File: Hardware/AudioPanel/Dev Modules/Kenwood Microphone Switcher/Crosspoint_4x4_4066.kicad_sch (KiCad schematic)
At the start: 53 parts, among them U201 4066, U202 4066, U203 4066, U204 4066, U205 74HC14, U206 74HC14, U207 74HC14

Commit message: Changed LEDs to 0603 SMDs
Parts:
- D201, D202, D203, D204, D205, D206, D207, D208, D209, D210, D211, D212, D213, D214, D215, D216: footprint LED_THT:LED_D5.0mm -> LED_SMD:LED_0603_1608Metric
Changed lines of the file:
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@@
 			)
 		)
-		(property "Footprint" "LED_THT:LED_D5.0mm"
+		(property "Footprint" "LED_SMD:LED_0603_1608Metric"
 			(at 295.91 105.41 0)
 			(effects
@@
 			)
 		)
-		(property "Footprint" "LED_THT:LED_D5.0mm"
+		(property "Footprint" "LED_SMD:LED_0603_1608Metric"
 			(at 295.91 149.86 0)
 			(effects
@@
 			)
 		)
-		(property "Footprint" "LED_THT:LED_D5.0mm"
+		(property "Footprint" "LED_SMD:LED_0603_1608Metric"
 			(at 295.91 142.24 0)
 			(effects
@@
 			)
 		)
-		(property "Footprint" "LED_THT:LED_D5.0mm"
+		(property "Footprint" "LED_SMD:LED_0603_1608Metric"
 			(at 295.91 69.85 0)
 			(effects
@@
 			)
 		)
-		(property "Footprint" "LED_THT:LED_D5.0mm"
+		(property "Footprint" "LED_SMD:LED_0603_1608Metric"
 			(at 295.91 90.17 0)
 			(effects
@@
 			)
 		)
-		(property "Footprint" "LED_THT:LED_D5.0mm"
+		(property "Footprint" "LED_SMD:LED_0603_1608Metric"
 			(at 295.91 120.65 0)
 			(effects
@@
 			)
 		)
-		(property "Footprint" "LED_THT:LED_D5.0mm"
+		(property "Footprint" "LED_SMD:LED_0603_1608Metric"
 			(at 295.91 97.79 0)
 			(effects
@@
 			)
 		)
-		(property "Footprint" "LED_THT:LED_D5.0mm"
+		(property "Footprint" "LED_SMD:LED_0603_1608Metric"
 			(at 295.91 62.23 0)
 			(effects
@@
 			)
 		)
-		(property "Footprint" "LED_THT:LED_D5.0mm"
+		(property "Footprint" "LED_SMD:LED_0603_1608Metric"
 			(at 295.91 157.48 0)
 			(effects
@@
 			)
 		)
-		(property "Footprint" "LED_THT:LED_D5.0mm"
+		(property "Footprint" "LED_SMD:LED_0603_1608Metric"
 			(at 295.91 113.03 0)
 			(effects
@@
 			)
 		)
-		(property "Footprint" "LED_THT:LED_D5.0mm"
+		(property "Footprint" "LED_SMD:LED_0603_1608Metric"
 			(at 295.91 31.75 0)
 			(effects
@@
 			)
 		)
-		(property "Footprint" "LED_THT:LED_D5.0mm"
+		(property "Footprint" "LED_SMD:LED_0603_1608Metric"
 			(at 295.91 54.61 0)
 			(effects
@@
 			)
 		)
-		(property "Footprint" "LED_THT:LED_D5.0mm"
+		(property "Footprint" "LED_SMD:LED_0603_1608Metric"
 			(at 295.91 46.99 0)
 			(effects
@@
 			)
 		)
-		(property "Footprint" "LED_THT:LED_D5.0mm"
+		(property "Footprint" "LED_SMD:LED_0603_1608Metric"
 			(at 295.91 82.55 0)
 			(effects
@@
 			)
 		)
-		(property "Footprint" "LED_THT:LED_D5.0mm"
+		(property "Footprint" "LED_SMD:LED_0603_1608Metric"
 			(at 295.91 39.37 0)
 			(effects
@@
 			)
 		)
-		(property "Footprint" "LED_THT:LED_D5.0mm"
+		(property "Footprint" "LED_SMD:LED_0603_1608Metric"
 			(at 295.91 134.62 0)
 			(effects

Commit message: Changed resistor arrays to SMD
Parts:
- RN201, RN202, RN203, RN204: footprint Resistor_THT:R_Array_SIP5 -> Resistor_SMD:R_Array_Concave_4x0402
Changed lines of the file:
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@@
 			)
 		)
-		(property "Footprint" "Resistor_THT:R_Array_SIP5"
+		(property "Footprint" "Resistor_SMD:R_Array_Concave_4x0402"
 			(at 167.64 52.832 90)
 			(effects
@@
 			)
 		)
-		(property "Footprint" "Resistor_THT:R_Array_SIP5"
+		(property "Footprint" "Resistor_SMD:R_Array_Concave_4x0402"
 			(at 167.64 47.752 90)
 			(effects
@@
 			)
 		)
-		(property "Footprint" "Resistor_THT:R_Array_SIP5"
+		(property "Footprint" "Resistor_SMD:R_Array_Concave_4x0402"
 			(at 167.64 27.432 90)
 			(effects
@@
 			)
 		)
-		(property "Footprint" "Resistor_THT:R_Array_SIP5"
+		(property "Footprint" "Resistor_SMD:R_Array_Concave_4x0402"
 			(at 167.64 32.512 90)
 			(effects
@@
 			)
 		)
-		(property "Footprint" "Resistor_THT:R_Array_SIP5"
+		(property "Footprint" "Resistor_SMD:R_Array_Concave_4x0402"
 			(at 167.64 40.132 90)
 			(effects
@@
 			)
 		)
-		(property "Footprint" "Resistor_THT:R_Array_SIP5"
+		(property "Footprint" "Resistor_SMD:R_Array_Concave_4x0402"
 			(at 167.64 65.532 90)
 			(effects
@@
 			)
 		)
-		(property "Footprint" "Resistor_THT:R_Array_SIP5"
+		(property "Footprint" "Resistor_SMD:R_Array_Concave_4x0402"
 			(at 167.64 37.592 90)
 			(effects
@@
 			)
 		)
-		(property "Footprint" "Resistor_THT:R_Array_SIP5"
+		(property "Footprint" "Resistor_SMD:R_Array_Concave_4x0402"
 			(at 167.64 62.992 90)
 			(effects
@@
 			)
 		)
-		(property "Footprint" "Resistor_THT:R_Array_SIP5"
+		(property "Footprint" "Resistor_SMD:R_Array_Concave_4x0402"
 			(at 167.64 45.212 90)
 			(effects
@@
 			)
 		)
-		(property "Footprint" "Resistor_THT:R_Array_SIP5"
+		(property "Footprint" "Resistor_SMD:R_Array_Concave_4x0402"
 			(at 167.64 29.972 90)
 			(effects
@@
 			)
 		)
-		(property "Footprint" "Resistor_THT:R_Array_SIP5"
+		(property "Footprint" "Resistor_SMD:R_Array_Concave_4x0402"
 			(at 167.64 57.912 90)
 			(effects
@@
 			)
 		)
-		(property "Footprint" "Resistor_THT:R_Array_SIP5"
+		(property "Footprint" "Resistor_SMD:R_Array_Concave_4x0402"
 			(at 167.64 35.052 90)
 			(effects
@@
 			)
 		)
-		(property "Footprint" "Resistor_THT:R_Array_SIP5"
+		(property "Footprint" "Resistor_SMD:R_Array_Concave_4x0402"
 			(at 167.64 50.292 90)
 			(effects
@@
 			)
 		)
-		(property "Footprint" "Resistor_THT:R_Array_SIP5"
+		(property "Footprint" "Resistor_SMD:R_Array_Concave_4x0402"
 			(at 167.64 42.672 90)
 			(effects
@@
 			)
 		)
-		(property "Footprint" "Resistor_THT:R_Array_SIP5"
+		(property "Footprint" "Resistor_SMD:R_Array_Concave_4x0402"
 			(at 167.64 60.452 90)
 			(effects
@@
 			)
 		)
-		(property "Footprint" "Resistor_THT:R_Array_SIP5"
+		(property "Footprint" "Resistor_SMD:R_Array_Concave_4x0402"
 			(at 167.64 55.372 90)
 			(effects

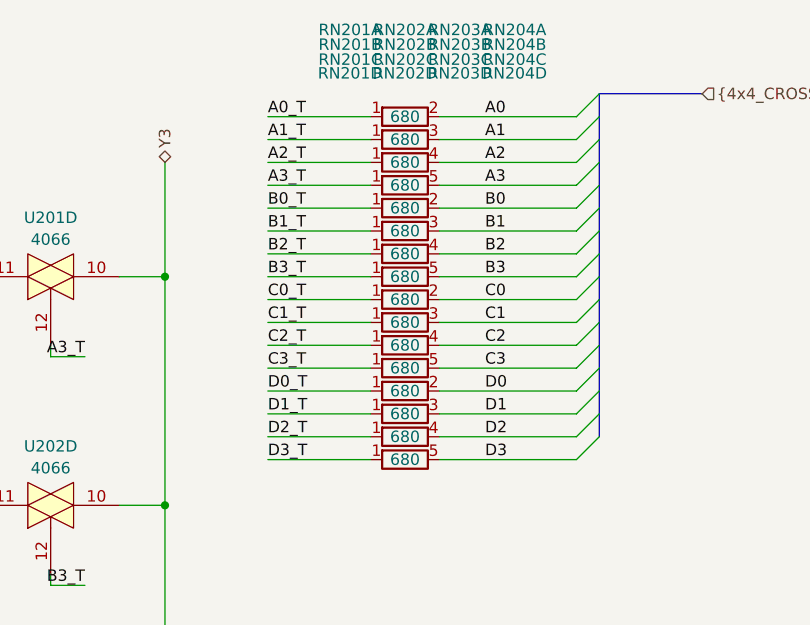
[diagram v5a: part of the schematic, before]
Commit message: Finished assigning footprints
No errors in PCB import, woo!
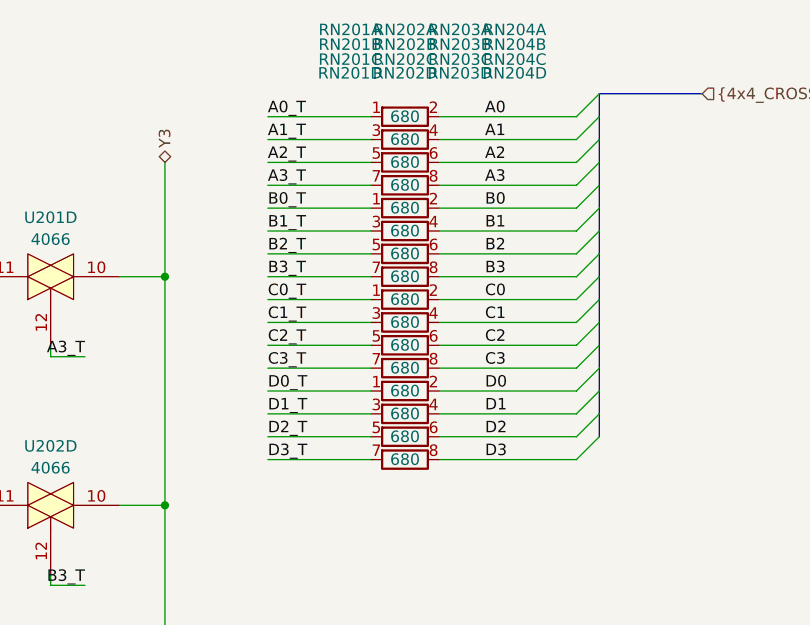
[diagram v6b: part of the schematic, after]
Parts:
- RN201, RN202, RN203, RN204: footprint Resistor_SMD:R_Array_Concave_4x0402 -> Resistor_SMD:R_Array_Convex_4x1206; symbol Device:R_Network04_Split -> Library_MicSwitcher:R_Network04_Split
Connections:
- net A1: now also RN201.4; no longer RN201.3 (R2.2)
- net A1_T: now also RN201.3; no longer RN201.1 (R1)
- net A2: now also RN201.6; no longer RN201.4 (R3.2)
- net A2_T: now also RN201.5; no longer RN201.1 (R1)
- net A3: now also RN201.8; no longer RN201.5 (R4.2)
- net A3_T: now also RN201.7; no longer RN201.1 (R1)
- net B1: now also RN202.4; no longer RN202.3 (R2.2)
- net B1_T: now also RN202.3; no longer RN202.1 (R1)
- net B2: now also RN202.6; no longer RN202.4 (R3.2)
- net B2_T: now also RN202.5; no longer RN202.1 (R1)
- net B3: now also RN202.8; no longer RN202.5 (R4.2)
- net B3_T: now also RN202.7; no longer RN202.1 (R1)
- net C1: now also RN203.4; no longer RN203.3 (R2.2)
- net C1_T: now also RN203.3; no longer RN203.1 (R1)
- net C2: now also RN203.6; no longer RN203.4 (R3.2)
- net C2_T: now also RN203.5; no longer RN203.1 (R1)
- net C3: now also RN203.8; no longer RN203.5 (R4.2)
- net C3_T: now also RN203.7; no longer RN203.1 (R1)
- net D1: now also RN204.4; no longer RN204.3 (R2.2)
- net D1_T: now also RN204.3; no longer RN204.1 (R1)
- net D2: now also RN204.6; no longer RN204.4 (R3.2)
- net D2_T: now also RN204.5; no longer RN204.1 (R1)
- net D3: now also RN204.8; no longer RN204.5 (R4.2)
- net D3_T: now also RN204.7; no longer RN204.1 (R1)
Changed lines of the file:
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@@
 	)
 	(symbol
-		(lib_id "Device:R_Network04_Split")
+		(lib_id "Library_MicSwitcher:R_Network04_Split")
 		(at 167.64 50.8 90)
 		(unit 3)
@@
 			)
 		)
-		(property "Footprint" "Resistor_SMD:R_Array_Concave_4x0402"
+		(property "Footprint" "Resistor_SMD:R_Array_Convex_4x1206"
 			(at 167.64 52.832 90)
 			(effects
@@
 		(pin "2"
 		)
+		(pin "7"
+		)
+		(pin "6"
+		)
+		(pin "8"
+		)
 		(instances
 			(project "Kenwood Microphone Switcher"
@@
 	)
 	(symbol
-		(lib_id "Device:R_Network04_Split")
+		(lib_id "Library_MicSwitcher:R_Network04_Split")
 		(at 167.64 45.72 90)
 		(unit 1)
@@
 			)
 		)
-		(property "Footprint" "Resistor_SMD:R_Array_Concave_4x0402"
+		(property "Footprint" "Resistor_SMD:R_Array_Convex_4x1206"
 			(at 167.64 47.752 90)
 			(effects
@@
 		(pin "2"
 		)
+		(pin "8"
+		)
+		(pin "6"
+		)
+		(pin "7"
+		)
 		(instances
 			(project "Kenwood Microphone Switcher"
@@
 	)
 	(symbol
-		(lib_id "Device:R_Network04_Split")
+		(lib_id "Library_MicSwitcher:R_Network04_Split")
 		(at 167.64 25.4 90)
 		(unit 1)
@@
 			)
 		)
-		(property "Footprint" "Resistor_SMD:R_Array_Concave_4x0402"
+		(property "Footprint" "Resistor_SMD:R_Array_Convex_4x1206"
 			(at 167.64 27.432 90)
 			(effects
@@
 		(pin "2"
 		)
+		(pin "6"
+		)
+		(pin "8"
+		)
+		(pin "7"
+		)
 		(instances
 			(project ""
@@
 	)
 	(symbol
-		(lib_id "Device:R_Network04_Split")
+		(lib_id "Library_MicSwitcher:R_Network04_Split")
 		(at 167.64 30.48 90)
 		(unit 3)
@@
 			)
 		)
-		(property "Footprint" "Resistor_SMD:R_Array_Concave_4x0402"
+		(property "Footprint" "Resistor_SMD:R_Array_Convex_4x1206"
 			(at 167.64 32.512 90)
 			(effects
@@
 		(pin "2"
 		)
+		(pin "8"
+		)
+		(pin "7"
+		)
+		(pin "6"
+		)
 		(instances
 			(project ""
@@
 	)
 	(symbol
-		(lib_id "Device:R_Network04_Split")
+		(lib_id "Library_MicSwitcher:R_Network04_Split")
 		(at 167.64 38.1 90)
 		(unit 2)
@@
 			)
 		)
-		(property "Footprint" "Resistor_SMD:R_Array_Concave_4x0402"
+		(property "Footprint" "Resistor_SMD:R_Array_Convex_4x1206"
 			(at 167.64 40.132 90)
 			(effects
@@
 		(pin "2"
 		)
+		(pin "7"
+		)
+		(pin "6"
+		)
+		(pin "8"
+		)
 		(instances
 			(project "Kenwood Microphone Switcher"
@@
 	)
 	(symbol
-		(lib_id "Device:R_Network04_Split")
+		(lib_id "Library_MicSwitcher:R_Network04_Split")
 		(at 167.64 63.5 90)
 		(unit 4)
@@
 			)
 		)
-		(property "Footprint" "Resistor_SMD:R_Array_Concave_4x0402"
+		(property "Footprint" "Resistor_SMD:R_Array_Convex_4x1206"
 			(at 167.64 65.532 90)
 			(effects
@@
 		(pin "2"
 		)
+		(pin "8"
+		)
+		(pin "6"
+		)
+		(pin "7"
+		)
 		(instances
 			(project "Kenwood Microphone Switcher"
@@
 	)
 	(symbol
-		(lib_id "Device:R_Network04_Split")
+		(lib_id "Library_MicSwitcher:R_Network04_Split")
 		(at 167.64 35.56 90)
 		(unit 1)
@@
 			)
 		)
-		(property "Footprint" "Resistor_SMD:R_Array_Concave_4x0402"
+		(property "Footprint" "Resistor_SMD:R_Array_Convex_4x1206"
 			(at 167.64 37.592 90)
 			(effects
@@
 		(pin "2"
 		)
+		(pin "6"
+		)
+		(pin "7"
+		)
+		(pin "8"
+		)
 		(instances
 			(project "Kenwood Microphone Switcher"
@@
 		(dnp no)
 		(fields_autoplaced yes)
-		(property "Reference" "#PWR0215"
+		(property "Reference" "#PWR0213"
 			(at 311.15 172.72 0)
 			(effects
@@
 			(project "Kenwood Microphone Switcher"
 				(path "/19b5c763-986e-434c-80ff-b1ac9c189e0e/08a77cad-86d7-4f50-8517-cb6e2e11f987"
-					(reference "#PWR0215")
+					(reference "#PWR0213")
 					(unit 1)
 				)
@@
 	)
 	(symbol
-		(lib_id "Device:R_Network04_Split")
+		(lib_id "Library_MicSwitcher:R_Network04_Split")
 		(at 167.64 60.96 90)
 		(unit 3)
@@
 			)
 		)
-		(property "Footprint" "Resistor_SMD:R_Array_Concave_4x0402"
+		(property "Footprint" "Resistor_SMD:R_Array_Convex_4x1206"
 			(at 167.64 62.992 90)
 			(effects
@@
 		(pin "2"
 		)
+		(pin "6"
+		)
+		(pin "8"
+		)
+		(pin "7"
+		)
 		(instances
 			(project "Kenwood Microphone Switcher"
@@
 	)
 	(symbol
-		(lib_id "Device:R_Network04_Split")
+		(lib_id "Library_MicSwitcher:R_Network04_Split")
 		(at 167.64 43.18 90)
 		(unit 4)
@@
 			)
 		)
-		(property "Footprint" "Resistor_SMD:R_Array_Concave_4x0402"
+		(property "Footprint" "Resistor_SMD:R_Array_Convex_4x1206"
 			(at 167.64 45.212 90)
 			(effects
@@
 		(pin "2"
 		)
+		(pin "7"
+		)
+		(pin "6"
+		)
+		(pin "8"
+		)
 		(instances
 			(project "Kenwood Microphone Switcher"
@@
 	)
 	(symbol
-		(lib_id "Device:R_Network04_Split")
+		(lib_id "Library_MicSwitcher:R_Network04_Split")
 		(at 167.64 27.94 90)
 		(unit 2)
@@
 			)
 		)
-		(property "Footprint" "Resistor_SMD:R_Array_Concave_4x0402"
+		(property "Footprint" "Resistor_SMD:R_Array_Convex_4x1206"
 			(at 167.64 29.972 90)
 			(effects
@@
 		(pin "2"
 		)
+		(pin "6"
+		)
+		(pin "7"
+		)
+		(pin "8"
+		)
 		(instances
 			(project ""
@@
 	)
 	(symbol
-		(lib_id "Device:R_Network04_Split")
+		(lib_id "Library_MicSwitcher:R_Network04_Split")
 		(at 167.64 55.88 90)
 		(unit 1)
@@
 			)
 		)
-		(property "Footprint" "Resistor_SMD:R_Array_Concave_4x0402"
+		(property "Footprint" "Resistor_SMD:R_Array_Convex_4x1206"
 			(at 167.64 57.912 90)
 			(effects
@@
 		(pin "2"
 		)
+		(pin "6"
+		)
+		(pin "8"
+		)
+		(pin "7"
+		)
 		(instances
 			(project "Kenwood Microphone Switcher"
@@
 	)
 	(symbol
-		(lib_id "Device:R_Network04_Split")
+		(lib_id "Library_MicSwitcher:R_Network04_Split")
 		(at 167.64 33.02 90)
 		(unit 4)
@@
 			)
 		)
-		(property "Footprint" "Resistor_SMD:R_Array_Concave_4x0402"
+		(property "Footprint" "Resistor_SMD:R_Array_Convex_4x1206"
 			(at 167.64 35.052 90)
 			(effects
@@
 		(pin "2"
 		)
+		(pin "8"
+		)
+		(pin "6"
+		)
+		(pin "7"
+		)
 		(instances
 			(project ""
@@
 		(dnp no)
 		(fields_autoplaced yes)
-		(property "Reference" "#PWR0213"
+		(property "Reference" "#PWR0211"
 			(at 311.15 69.85 0)
 			(effects
@@
 			(project "Kenwood Microphone Switcher"
 				(path "/19b5c763-986e-434c-80ff-b1ac9c189e0e/08a77cad-86d7-4f50-8517-cb6e2e11f987"
-					(reference "#PWR0213")
+					(reference "#PWR0211")
 					(unit 1)
 				)
@@
 	)
 	(symbol
-		(lib_id "Device:R_Network04_Split")
+		(lib_id "Library_MicSwitcher:R_Network04_Split")
 		(at 167.64 48.26 90)
 		(unit 2)
@@
 			)
 		)
-		(property "Footprint" "Resistor_SMD:R_Array_Concave_4x0402"
+		(property "Footprint" "Resistor_SMD:R_Array_Convex_4x1206"
 			(at 167.64 50.292 90)
 			(effects
@@
 		(pin "2"
 		)
+		(pin "6"
+		)
+		(pin "7"
+		)
+		(pin "8"
+		)
 		(instances
 			(project "Kenwood Microphone Switcher"
@@
 	)
 	(symbol
-		(lib_id "Device:R_Network04_Split")
+		(lib_id "Library_MicSwitcher:R_Network04_Split")
 		(at 167.64 40.64 90)
 		(unit 3)
@@
 			)
 		)
-		(property "Footprint" "Resistor_SMD:R_Array_Concave_4x0402"
+		(property "Footprint" "Resistor_SMD:R_Array_Convex_4x1206"
 			(at 167.64 42.672 90)
 			(effects
@@
 		(pin "2"
 		)
+		(pin "6"
+		)
+		(pin "8"
+		)
+		(pin "7"
+		)
 		(instances
 			(project "Kenwood Microphone Switcher"
@@
 	)
 	(symbol
-		(lib_id "Device:R_Network04_Split")
+		(lib_id "Library_MicSwitcher:R_Network04_Split")
 		(at 167.64 58.42 90)
 		(unit 2)
@@
 			)
 		)
-		(property "Footprint" "Resistor_SMD:R_Array_Concave_4x0402"
+		(property "Footprint" "Resistor_SMD:R_Array_Convex_4x1206"
 			(at 167.64 60.452 90)
 			(effects
@@
 		(pin "2"
 		)
+		(pin "7"
+		)
+		(pin "6"
+		)
+		(pin "8"
+		)
 		(instances
 			(project "Kenwood Microphone Switcher"
@@
 	)
 	(symbol
-		(lib_id "Device:R_Network04_Split")
+		(lib_id "Library_MicSwitcher:R_Network04_Split")
 		(at 167.64 53.34 90)
 		(unit 4)
@@
 			)
 		)
-		(property "Footprint" "Resistor_SMD:R_Array_Concave_4x0402"
+		(property "Footprint" "Resistor_SMD:R_Array_Convex_4x1206"
 			(at 167.64 55.372 90)
 			(effects
@@
 		(pin "2"
 		)
+		(pin "6"
+		)
+		(pin "7"
+		)
+		(pin "8"
+		)
 		(instances
 			(project "Kenwood Microphone Switcher"
@@
 		(dnp no)
 		(fields_autoplaced yes)
-		(property "Reference" "#PWR0214"
+		(property "Reference" "#PWR0212"
 			(at 311.15 120.65 0)
 			(effects
@@
 			(project "Kenwood Microphone Switcher"
 				(path "/19b5c763-986e-434c-80ff-b1ac9c189e0e/08a77cad-86d7-4f50-8517-cb6e2e11f987"
-					(reference "#PWR0214")
+					(reference "#PWR0212")
 					(unit 1)
 				)

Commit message: Started work on COM switching dev board
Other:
- company: (none) -> Thomas Francois - KX∅STL
- title: (none) -> Kenwood Handset Switcher - Dev Board
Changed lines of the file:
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@@
 	(generator_version "9.0")
 	(paper "B")
+	(title_block
+		(title "Kenwood Handset Switcher - Dev Board")
+		(date "2025-07-11")
+		(rev "A")
+		(company "Thomas Francois - KX∅STL")
+	)
 	(junction
 		(at 304.8 120.65)
